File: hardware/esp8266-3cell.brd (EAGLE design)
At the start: 26.6 x 34.3 mm, 10 parts, among them IC1 MCP1603, J1 HEADER_10P, J2 HEADER_10P, J3 HEADER_3P, J4 HEADER_3P

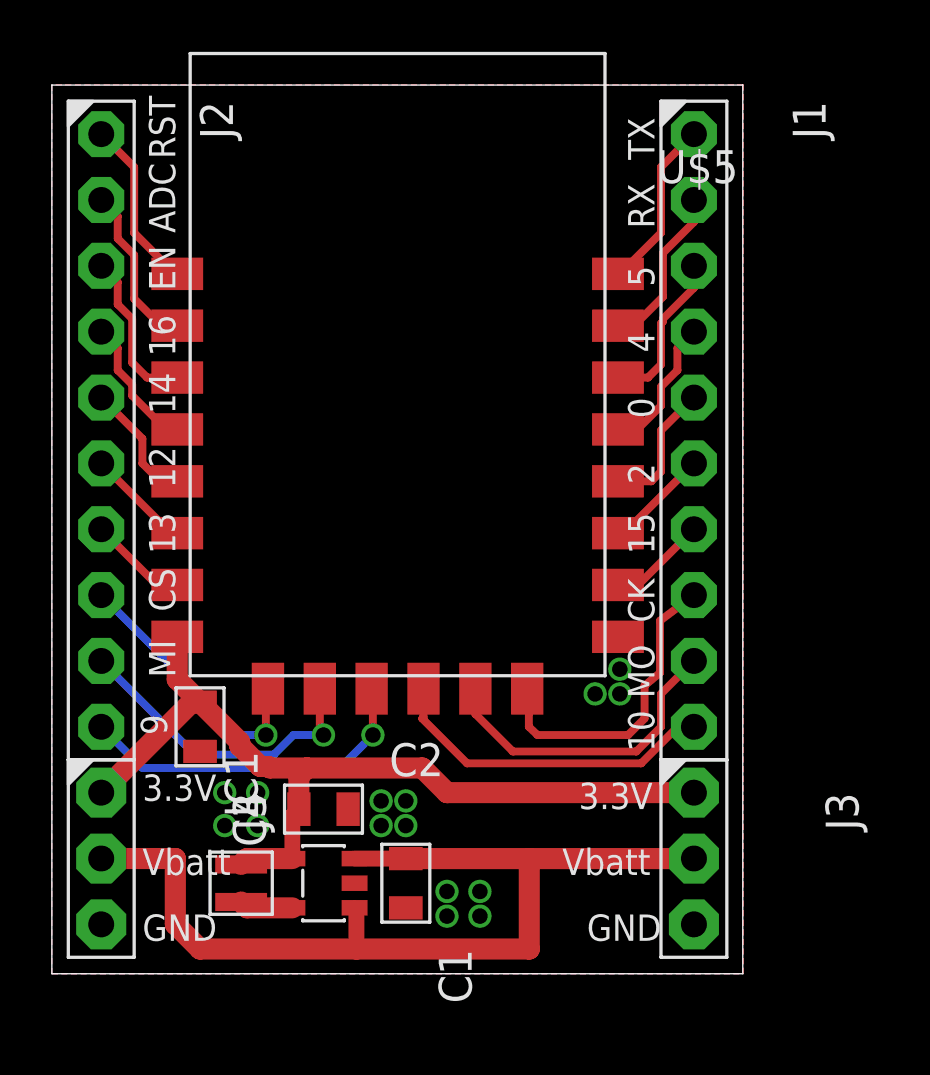
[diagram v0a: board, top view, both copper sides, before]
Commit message: improved layout near input capacitor
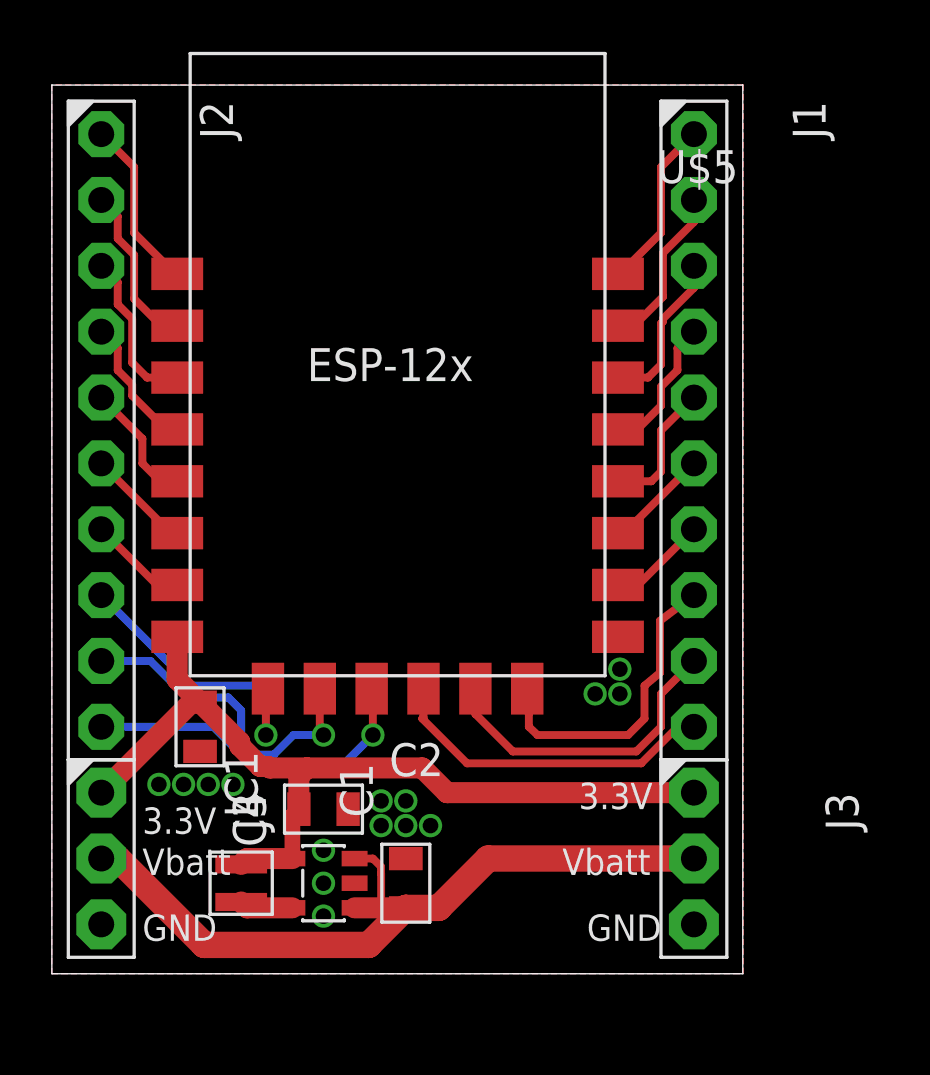
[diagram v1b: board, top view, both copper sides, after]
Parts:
- turned C1 to 90 degrees
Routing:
- net VBATT: track 37.6 -> 30.4 mm
- net CS0: track 10.4 -> 11.5 mm
- net MISO: track 12.2 -> 12.9 mm
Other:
- board text added: "3/10/2018"
- board text added: "CS0"
- board text added: "ESP-12x"
- board text added: "ESP8266-3Cell"
- board text added: "GPIO0"
- board text added: "GPIO10"
- board text added: "GPIO12"
- board text added: "GPIO13"
- board text added: "GPIO14"
- board text added: "GPIO15"
- board text added: "GPIO16"
- board text added: "GPIO2"
- board text added: "GPIO4"
- board text added: "GPIO5"
- board text added: "GPIO9"
- board text added: "MISO"
- board text added: "MOSI"
- board text added: "RXD"
- board text added: "SCLK"
- board text added: "TCY"
- board text added: "TXD"
- board text added: "V1.1"
- board text removed: "0"
- board text removed: "10"
- board text removed: "12"
- board text removed: "13"
- board text removed: "14"
- board text removed: "15"
- board text removed: "16"
- board text removed: "2"
- board text removed: "4"
- board text removed: "5"
- board text removed: "9"
- board text removed: "CK"
- board text removed: "CS"
- board text removed: "MI"
- board text removed: "MO"
- board text removed: "RX"
- board text removed: "TX"
